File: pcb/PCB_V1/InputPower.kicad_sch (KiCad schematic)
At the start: 14 parts, among them J901 12 V IN / 25 A design, Q901 P-MOSFET reverse-polarity / M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

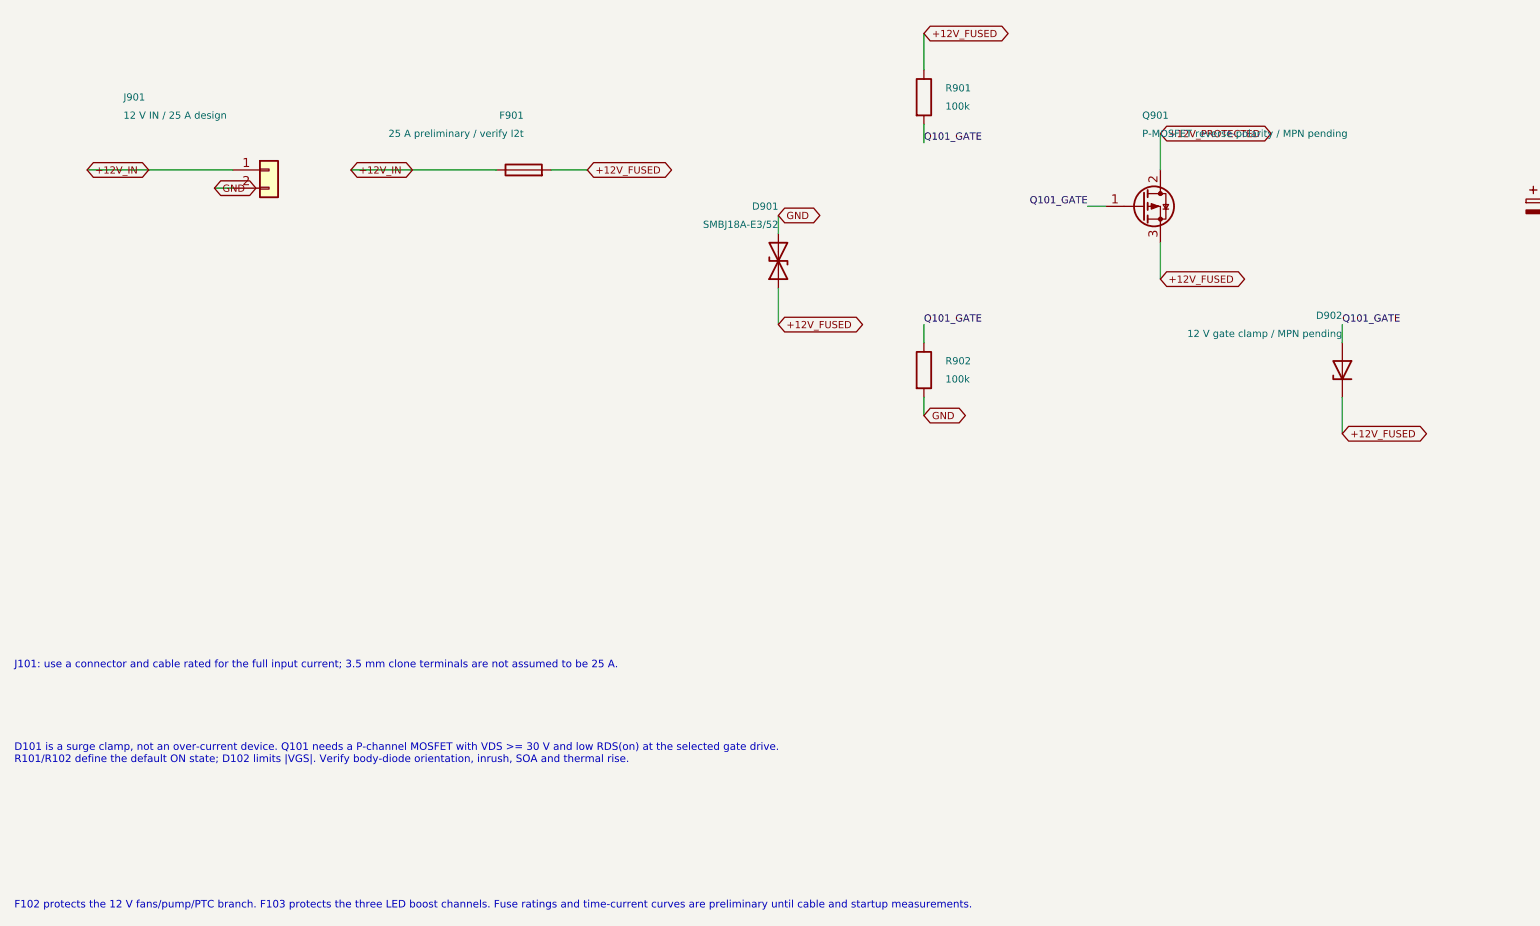
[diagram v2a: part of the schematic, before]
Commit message: pcb: stage four-layer board and enforce unique references
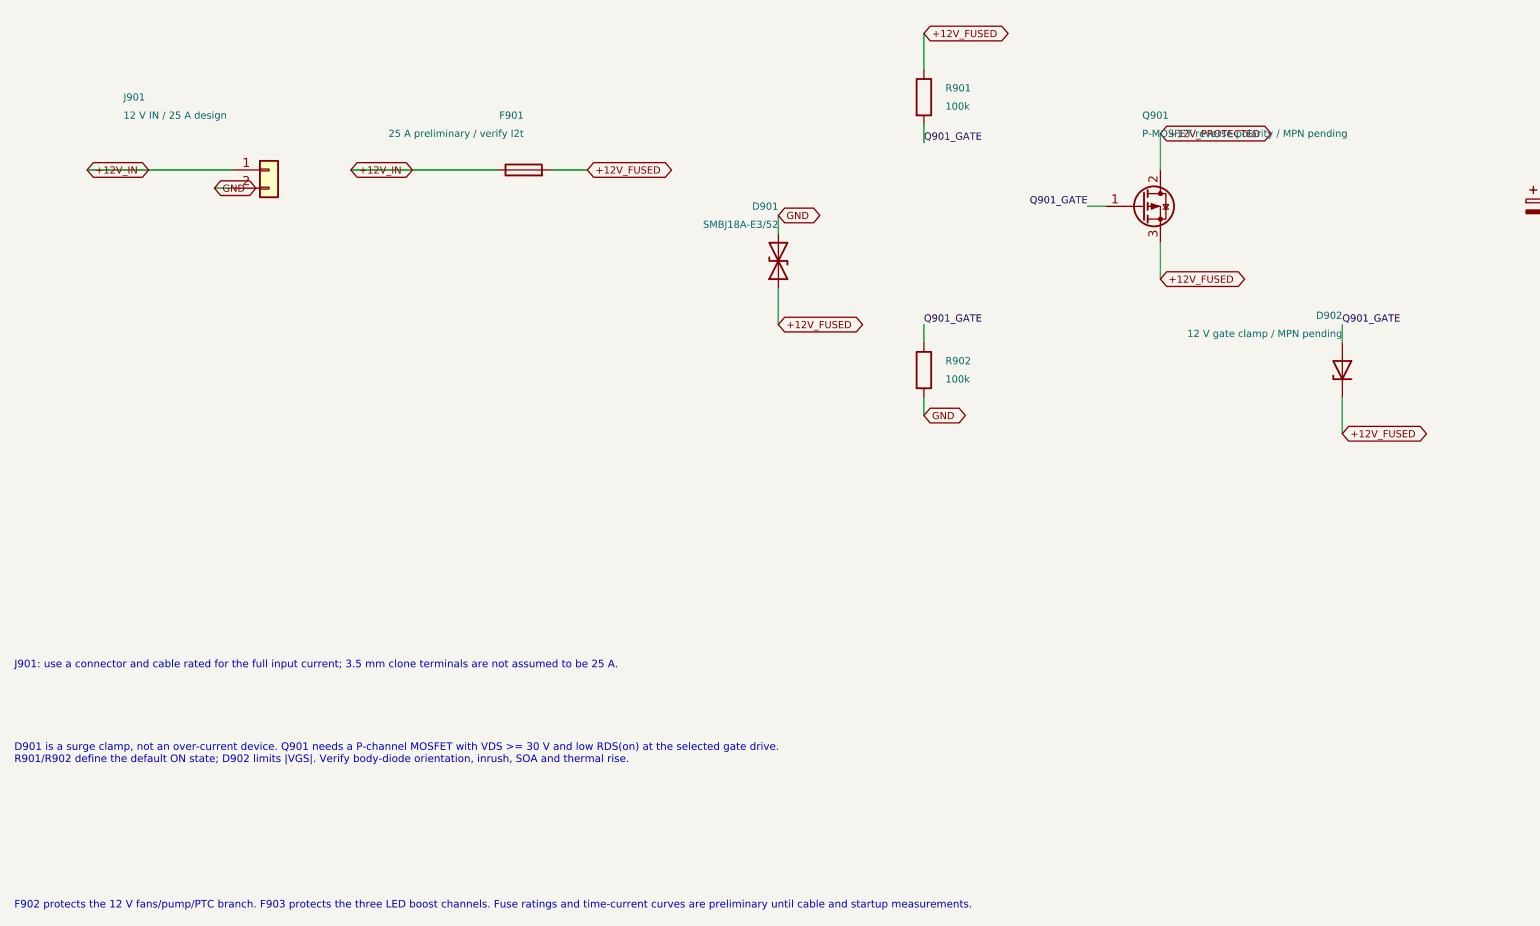
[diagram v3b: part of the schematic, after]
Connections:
- net Q101_GATE renamed Q901_GATE
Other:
- note added: "D901 is a surge clamp, not an over-current device. Q901 needs a P-channel MOSFET with VDS >= 30 V and low RDS(on) at the selected gate drive. R901/R902 define the default ON state; D902 limits |VGS|. Verify body-diode orientation, inrush, SOA and thermal rise."
- note added: "F902 protects the 12 V fans/pump/PTC branch. F903 protects the three LED boost channels. Fuse ratings and time-current curves are preliminary until cable and startup measurements."
- note added: "J901: use a connector and cable rated for the full input current; 3.5 mm clone terminals are not assumed to be 25 A."
- note removed: "D101 is a surge clamp, not an over-current device. Q101 needs a P-channel MOSFET with VDS >= 30 V and low RDS(on) at the selected gate drive. R101/R102 define the default ON state; D102 limits |VGS|. Verify body-diode orientation, inrush, SOA and thermal rise."
- note removed: "F102 protects the 12 V fans/pump/PTC branch. F103 protects the three LED boost channels. Fuse ratings and time-current curves are preliminary until cable and startup measurements."
- note removed: "J101: use a connector and cable rated for the full input current; 3.5 mm clone terminals are not assumed to be 25 A."

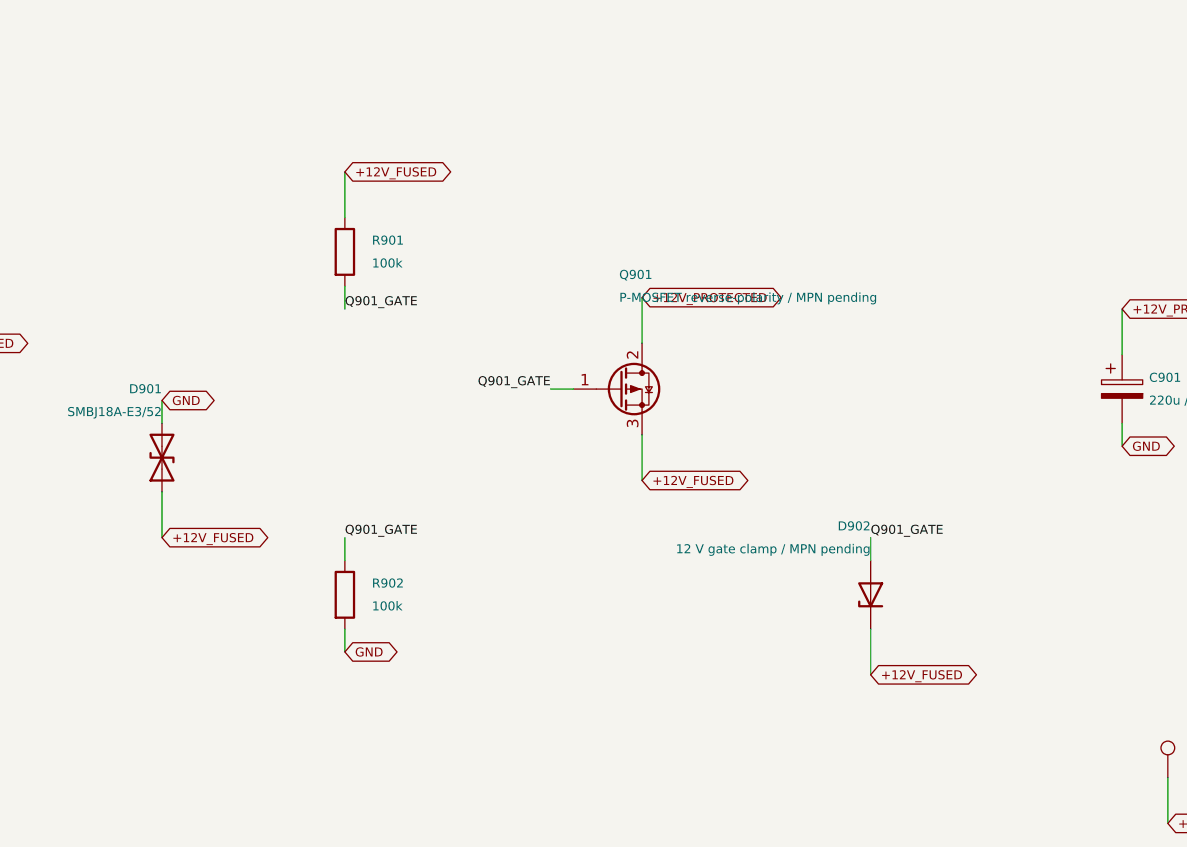
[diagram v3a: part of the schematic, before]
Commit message: pcb: correct power MOSFET pin mapping and reverse input protection
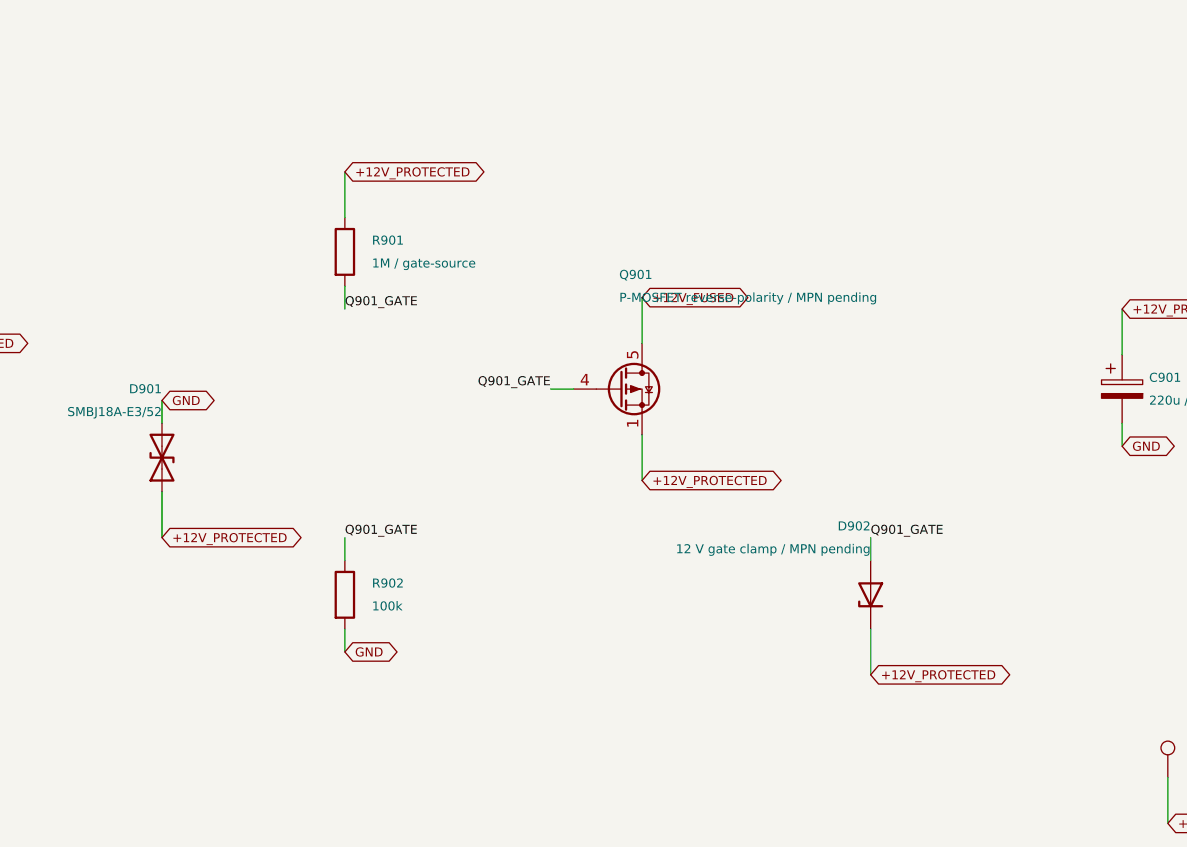
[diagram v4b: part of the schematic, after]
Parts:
- Q901: symbol Transistor_FET:Q_PMOS_GDS -> GrowBox:PMOS_PowerPAK_Candidate
- R901: value 100k -> 1M / gate-source
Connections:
- net +12V_FUSED: now also Q901.5 (D); no longer D901.1 (A1), D902.1 (K), Q901.3 (S), R901.1
- net +12V_PROTECTED: now also D901.1 (A1), D902.1 (K), Q901.1 (S), Q901.3 (S), R901.1
- net Q901_GATE: now also Q901.4 (G); no longer Q901.1 (G)
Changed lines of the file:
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@@
 		(title "06 - 12 V input protection and branch fuses")
 		(date "2026-09-26")
-		(rev "0.4-DRAFT")
+		(rev "0.7-DRAFT")
 		(company "GrowBox controller")
 		(comment 1 "Logic first; power loads not yet implemented")
@@
 		)
 	)
+	(global_label "+12V_FUSED"
+		(shape bidirectional)
+		(at 180.34 50.8 0)
+		(effects
+			(font
+				(size 1 1)
+			)
+			(justify left bottom)
+		)
+		(property "Intersheetrefs" "${INTERSHEET_REFS}"
+			(at 180.34 50.8 0)
+			(hide yes)
+			(show_name no)
+			(do_not_autoplace no)
+			(effects
+				(font
+					(size 1.27 1.27)
+				)
+			)
+		)
+	)
+	(global_label "+12V_IN"
+		(shape bidirectional)
+		(at 67.31 55.88 0)
+		(effects
+			(font
+				(size 1 1)
+			)
+			(justify left bottom)
+		)
+		(property "Intersheetrefs" "${INTERSHEET_REFS}"
+			(at 67.31 55.88 0)
+			(hide yes)
+			(show_name no)
+			(do_not_autoplace no)
+			(effects
+				(font
+					(size 1.27 1.27)
+				)
+			)
+		)
+	)
+	(global_label "GND"
+		(shape bidirectional)
+		(at 147.32 90.17 0)
+		(effects
+			(font
+				(size 1 1)
+			)
+			(justify left bottom)
+		)
+		(property "Intersheetrefs" "${INTERSHEET_REFS}"
+			(at 147.32 90.17 0)
+			(hide yes)
+			(show_name no)
+			(do_not_autoplace no)
+			(effects
+				(font
+					(size 1.27 1.27)
+				)
+			)
+		)
+	)
 	(global_label "+12V_PROTECTED"
 		(shape bidirectional)
-		(at 180.34 50.8 0)
-		(effects
-			(font
-				(size 1 1)
-			)
-			(justify left bottom)
-		)
-		(property "Intersheetrefs" "${INTERSHEET_REFS}"
-			(at 180.34 50.8 0)
-			(hide yes)
-			(show_name no)
-			(do_not_autoplace no)
-			(effects
-				(font
-					(size 1.27 1.27)
-				)
-			)
-		)
-	)
-	(global_label "+12V_IN"
-		(shape bidirectional)
-		(at 67.31 55.88 0)
-		(effects
-			(font
-				(size 1 1)
-			)
-			(justify left bottom)
-		)
-		(property "Intersheetrefs" "${INTERSHEET_REFS}"
-			(at 67.31 55.88 0)
+		(at 147.32 36.83 0)
+		(effects
+			(font
+				(size 1 1)
+			)
+			(justify left bottom)
+		)
+		(property "Intersheetrefs" "${INTERSHEET_REFS}"
+			(at 147.32 36.83 0)
+			(hide yes)
+			(show_name no)
+			(do_not_autoplace no)
+			(effects
+				(font
+					(size 1.27 1.27)
+				)
+			)
+		)
+	)
+	(global_label "+12V_PROTECTED"
+		(shape bidirectional)
+		(at 127 77.47 0)
+		(effects
+			(font
+				(size 1 1)
+			)
+			(justify left bottom)
+		)
+		(property "Intersheetrefs" "${INTERSHEET_REFS}"
+			(at 127 77.47 0)
 			(hide yes)
 			(show_name no)
@@
 	(global_label "GND"
 		(shape bidirectional)
-		(at 147.32 90.17 0)
-		(effects
-			(font
-				(size 1 1)
-			)
-			(justify left bottom)
-		)
-		(property "Intersheetrefs" "${INTERSHEET_REFS}"
-			(at 147.32 90.17 0)
-			(hide yes)
-			(show_name no)
-			(do_not_autoplace no)
-			(effects
-				(font
-					(size 1.27 1.27)
-				)
-			)
-		)
-	)
-	(global_label "+12V_FUSED"
-		(shape bidirectional)
-		(at 147.32 36.83 0)
-		(effects
-			(font
-				(size 1 1)
-			)
-			(justify left bottom)
-		)
-		(property "Intersheetrefs" "${INTERSHEET_REFS}"
-			(at 147.32 36.83 0)
-			(hide yes)
-			(show_name no)
-			(do_not_autoplace no)
-			(effects
-				(font
-					(size 1.27 1.27)
-				)
-			)
-		)
-	)
-	(global_label "+12V_FUSED"
-		(shape bidirectional)
-		(at 127 77.47 0)
-		(effects
-			(font
-				(size 1 1)
-			)
-			(justify left bottom)
-		)
-		(property "Intersheetrefs" "${INTERSHEET_REFS}"
-			(at 127 77.47 0)
-			(hide yes)
-			(show_name no)
-			(do_not_autoplace no)
-			(effects
-				(font
-					(size 1.27 1.27)
-				)
-			)
-		)
-	)
-	(global_label "GND"
-		(shape bidirectional)
 		(at 48.26 58.42 0)
 		(effects
@@
 		)
 	)
-	(global_label "+12V_FUSED"
+	(global_label "+12V_PROTECTED"
 		(shape bidirectional)
 		(at 180.34 71.12 0)
@@
 		)
 	)
-	(global_label "+12V_FUSED"
+	(global_label "+12V_PROTECTED"
 		(shape bidirectional)
 		(at 205.74 92.71 0)
@@
 	)
 	(symbol
-		(lib_id "Transistor_FET:Q_PMOS_GDS")
+		(lib_id "GrowBox:PMOS_PowerPAK_Candidate")
 		(at 177.8 60.96 0)
 		(unit 1)
@@
 				)
 			)
+		)
+		(pin "4"
+		)
+		(pin "5"
 		)
 		(pin "1"
@@
 			)
 		)
-		(property "Value" "100k"
+		(property "Value" "1M / gate-source"
 			(at 150.32 46.99 0)
 			(show_name no)
